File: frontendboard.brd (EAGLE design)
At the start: 160 x 100 mm, 65 parts, among them U1 MAX2769, X3 BU-SMA-H

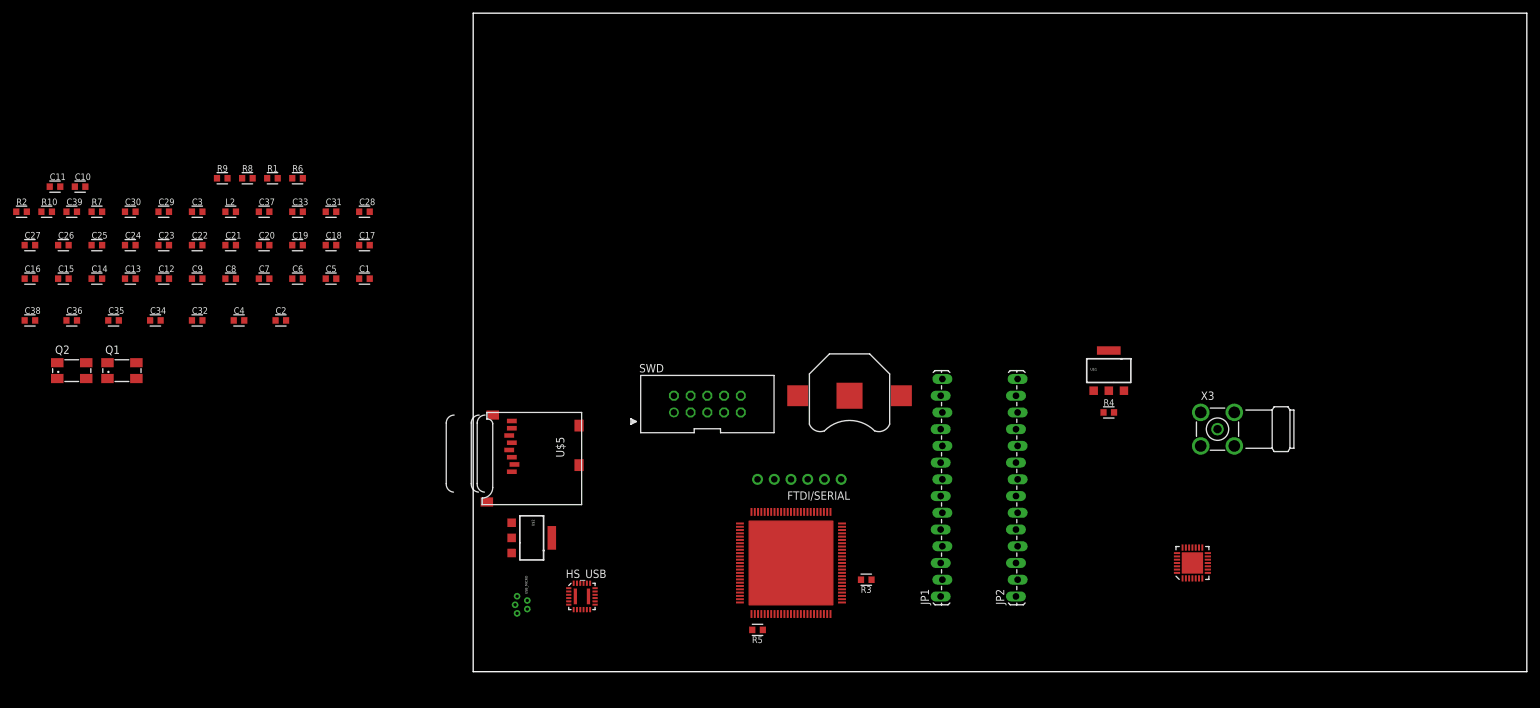
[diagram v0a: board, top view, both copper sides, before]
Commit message: Got all parts on the board for the layout. General sense of things.
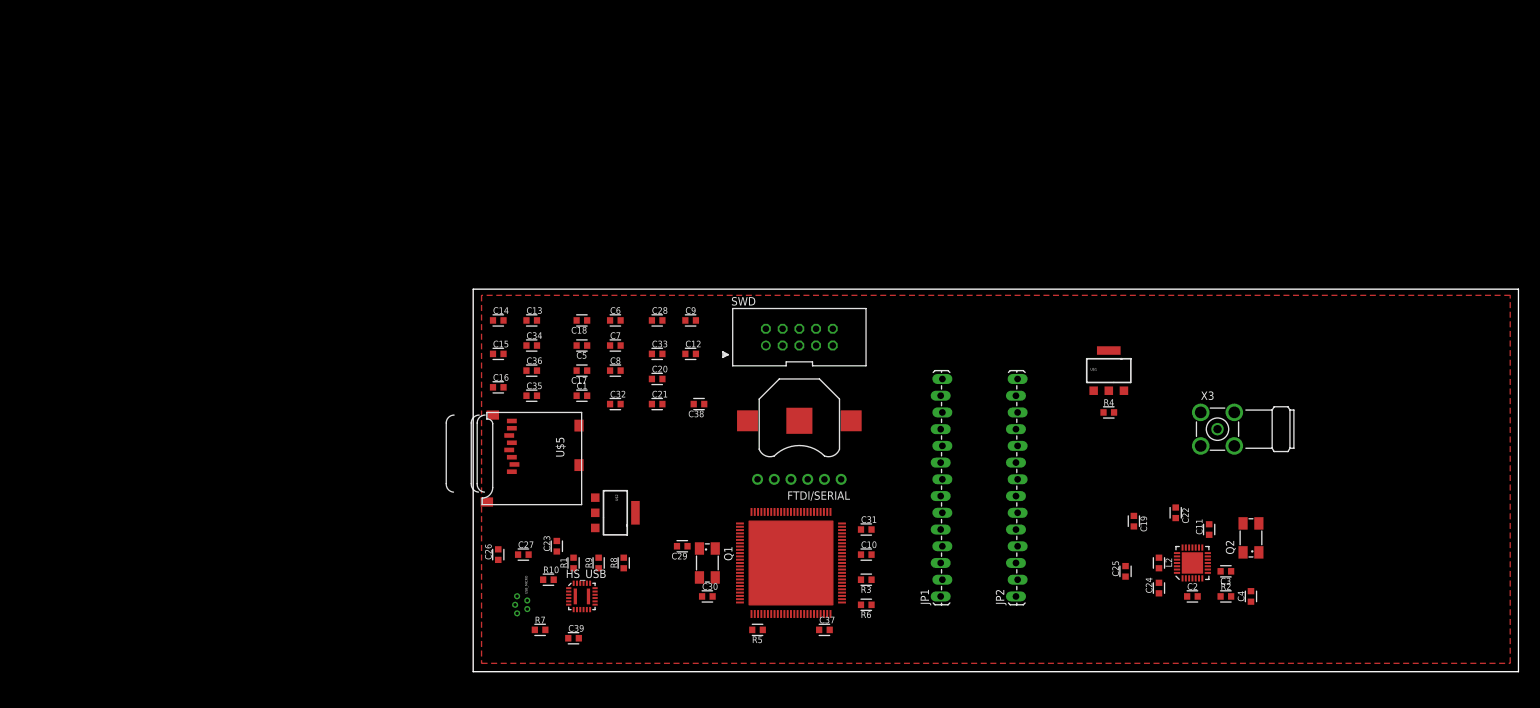
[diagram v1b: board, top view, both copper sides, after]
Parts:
- moved R2 192.0 mm to (114.3, 11.4)
- moved C11 182.8 mm to (111.8, 21.6), turned to 90 degrees
- moved Q2 180.9 mm to (118.1, 20.3), turned to 90 degrees
- moved C3 165.5 mm to (114.3, 15.2), turned to 180 degrees
- moved C24 164.7 mm to (104.1, 12.7), turned to 90 degrees
- moved C25 163.9 mm to (99.1, 15.2), turned to 90 degrees
- moved C4 159.3 mm to (118.1, 11.4), turned to 90 degrees
- moved C22 154.0 mm to (106.7, 24.1), turned to 270 degrees
- moved L2 150.7 mm to (104.1, 16.5), turned to 270 degrees
- moved C2 144.6 mm to (109.2, 11.4)
- moved C19 133.7 mm to (100.3, 22.9), turned to 270 degrees
- moved C10 131.8 mm to (59.7, 17.8)
- moved R6 108.0 mm to (59.7, 10.2), turned to 180 degrees
- moved C37 106.2 mm to (53.3, 6.35)
- moved C30 105.3 mm to (35.6, 11.4)
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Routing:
- added copper zone on layer 1, net BAR_GND
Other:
- board size 160 x 100 mm -> 158.7 x 58.1 mm

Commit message: Saving it before Andrew touches it.
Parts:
- removed C20: 0.1uF, rcl_custom:0603-B
- removed C21: 0.1nF, rcl_custom:0603-B
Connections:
- net 3.3VD: no longer C20.1, C21.1, Q2.1
- net BAR_GND: now also Q2.1; no longer C20.2, C21.2
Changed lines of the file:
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@@
 <element name="U$1" library="microbuilder" package="SOT223-R" value="" x="96.52" y="45.72"/>
 <element name="U$2" library="microbuilder" package="SOT223-R" value="" x="21.59" y="24.13" rot="R270"/>
-<element name="C20" library="rcl_custom" package="0603-B" value="0.1uF" x="27.94" y="44.45"/>
-<element name="C21" library="rcl_custom" package="0603-B" value="0.1nF" x="27.94" y="40.64"/>
 <element name="R4" library="rcl_custom" package="0603-B" value="20k" x="96.52" y="39.37"/>
 <element name="R5" library="rcl_custom" package="0603-B" value="20k" x="43.18" y="6.35" rot="R180"/>
@@
 <contactref element="U$2" pad="1"/>
 <contactref element="U$1" pad="1"/>
-<contactref element="C21" pad="2"/>
-<contactref element="C20" pad="2"/>
 <contactref element="R3" pad="1"/>
 <contactref element="R6" pad="1"/>
@@
 <vertex x="157.48" y="1.27"/>
 </polygon>
-<wire x1="58.89" y1="21.59" x2="56.01" y2="22.01" width="0" layer="19" extent="1-1"/>
+<contactref element="Q2" pad="1"/>
+<wire x1="118.11" y1="12.23" x2="119.31" y2="18.12" width="0" layer="19" extent="1-1"/>
+<wire x1="56.01" y1="22.01" x2="58.89" y2="21.59" width="0" layer="19" extent="1-1"/>
 <wire x1="17.51" y1="11.43" x2="19.05" y2="15.71" width="0" layer="19" extent="1-1"/>
 <wire x1="40.51" y1="13.01" x2="34.76" y2="11.43" width="0" layer="19" extent="1-1"/>
@@
 <contactref element="C9" pad="1"/>
 <contactref element="U1" pad="19"/>
-<contactref element="C20" pad="1"/>
-<contactref element="C21" pad="1"/>
-<contactref element="Q2" pad="1"/>
 <contactref element="R5" pad="2"/>
 <contactref element="HS_USB" pad="4"/>
@@
 <contactref element="C39" pad="2"/>
 <contactref element="U$3" pad="P$21"/>
-<wire x1="108.72" y1="18.85" x2="119.31" y2="18.12" width="0" layer="19" extent="1-1"/>
 <wire x1="56.01" y1="22.51" x2="108.72" y2="18.85" width="0" layer="19" extent="1-1"/>
 <wire x1="50.8" y1="29.21" x2="56.01" y2="22.51" width="0" layer="19" extent="1-1"/>
@@
 <wire x1="54.26" y1="8.76" x2="42.26" y2="8.76" width="0" layer="19" extent="1-1"/>
 <wire x1="33.49" y1="40.64" x2="42.26" y2="24.26" width="0" layer="19" extent="1-1"/>
-<wire x1="27.14" y1="40.64" x2="33.49" y2="40.64" width="0" layer="19" extent="1-1"/>
-<wire x1="27.14" y1="44.45" x2="27.14" y2="40.64" width="0" layer="19" extent="1-1"/>
-<wire x1="28.74" y1="48.26" x2="27.14" y2="44.45" width="0" layer="19" extent="1-1"/>
-<wire x1="22.39" y1="40.64" x2="27.14" y2="40.64" width="0" layer="19" extent="1-1"/>
+<wire x1="28.74" y1="48.26" x2="33.49" y2="40.64" width="0" layer="19" extent="1-1"/>
 <wire x1="28.74" y1="53.34" x2="28.74" y2="48.26" width="0" layer="19" extent="1-1"/>
 <wire x1="32.22" y1="53.34" x2="28.74" y2="53.34" width="0" layer="19" extent="1-1"/>
+<wire x1="22.39" y1="40.64" x2="28.74" y2="48.26" width="0" layer="19" extent="1-1"/>
 <wire x1="17.31" y1="41.91" x2="22.39" y2="40.64" width="0" layer="19" extent="1-1"/>
 <wire x1="17.31" y1="45.72" x2="17.31" y2="41.91" width="0" layer="19" extent="1-1"/>

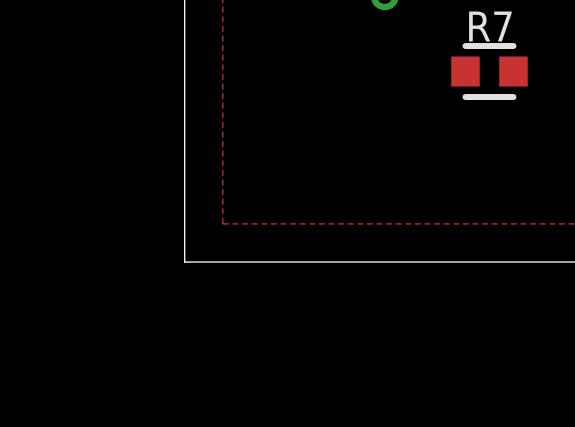
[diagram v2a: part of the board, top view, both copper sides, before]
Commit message: Add buses. Complete SDIO detect circuit. Add bypass caps where needed.
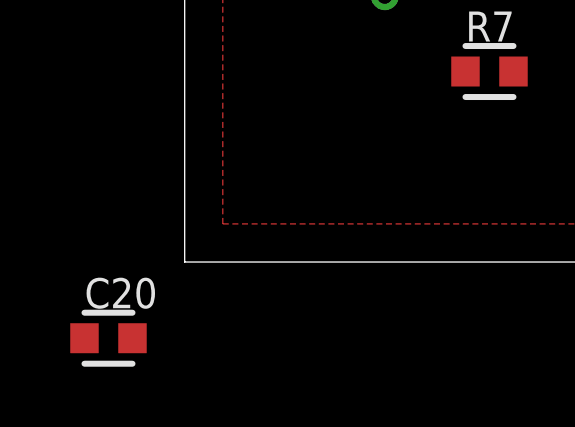
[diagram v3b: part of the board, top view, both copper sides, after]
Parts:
- added C20: 2.2uF, rcl_custom:0603-B
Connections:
- net 3.3VD: now also C20.2
- net BAR_GND: now also C20.1, U$5.CD2
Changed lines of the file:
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@@
 <attribute name="OC_FARNELL" value="unknown" x="163.83" y="81.28" size="1.778" layer="27" rot="R90" display="off"/>
 </element>
+<element name="C20" library="rcl_custom" package="0603-B" value="2.2uF" x="-2.54" y="-2.54"/>
 </elements>
 <signals>
@@
 </polygon>
 <contactref element="Q2" pad="1"/>
+<contactref element="C20" pad="1"/>
+<contactref element="U$5" pad="CD2"/>
+<wire x1="115.5799" y1="34.2801" x2="115.5799" y2="39.3799" width="0" layer="19" extent="1-1"/>
+<wire x1="110.4801" y1="39.3799" x2="115.5799" y2="39.3799" width="0" layer="19" extent="1-1"/>
+<wire x1="110.4801" y1="34.2801" x2="115.5799" y2="34.2801" width="0" layer="19" extent="1-1"/>
+<wire x1="119.31" y1="18.12" x2="115.5799" y2="34.2801" width="0" layer="19" extent="1-1"/>
 <wire x1="118.11" y1="12.23" x2="119.31" y2="18.12" width="0" layer="19" extent="1-1"/>
+<wire x1="113.5" y1="15.24" x2="118.11" y2="12.23" width="0" layer="19" extent="1-1"/>
+<wire x1="104.14" y1="13.5" x2="113.5" y2="15.24" width="0" layer="19" extent="1-1"/>
+<wire x1="99.06" y1="16.04" x2="104.14" y2="13.5" width="0" layer="19" extent="1-1"/>
+<wire x1="94.22" y1="42.67" x2="110.4801" y2="39.3799" width="0" layer="19" extent="1-1"/>
+<wire x1="60.49" y1="17.78" x2="99.06" y2="16.04" width="0" layer="19" extent="1-1"/>
+<wire x1="60.49" y1="13.97" x2="60.49" y2="17.78" width="0" layer="19" extent="1-1"/>
+<wire x1="60.49" y1="10.16" x2="60.49" y2="13.97" width="0" layer="19" extent="1-1"/>
+<wire x1="58.89" y1="21.59" x2="60.49" y2="17.78" width="0" layer="19" extent="1-1"/>
 <wire x1="56.01" y1="22.01" x2="58.89" y2="21.59" width="0" layer="19" extent="1-1"/>
+<wire x1="55.88" y1="29.21" x2="56.01" y2="22.01" width="0" layer="19" extent="1-1"/>
+<wire x1="52.54" y1="6.35" x2="60.49" y2="10.16" width="0" layer="19" extent="1-1"/>
+<wire x1="42.76" y1="8.76" x2="52.54" y2="6.35" width="0" layer="19" extent="1-1"/>
+<wire x1="40.51" y1="13.01" x2="42.76" y2="8.76" width="0" layer="19" extent="1-1"/>
+<wire x1="40.51" y1="18.01" x2="40.51" y2="13.01" width="0" layer="19" extent="1-1"/>
+<wire x1="34.76" y1="11.43" x2="40.51" y2="13.01" width="0" layer="19" extent="1-1"/>
+<wire x1="32.55" y1="19.05" x2="34.76" y2="11.43" width="0" layer="19" extent="1-1"/>
+<wire x1="22.86" y1="15.71" x2="32.55" y2="19.05" width="0" layer="19" extent="1-1"/>
+<wire x1="19.05" y1="15.71" x2="22.86" y2="15.71" width="0" layer="19" extent="1-1"/>
 <wire x1="17.51" y1="11.43" x2="19.05" y2="15.71" width="0" layer="19" extent="1-1"/>
-<wire x1="40.51" y1="13.01" x2="34.76" y2="11.43" width="0" layer="19" extent="1-1"/>
-<wire x1="42.76" y1="8.76" x2="40.51" y2="13.01" width="0" layer="19" extent="1-1"/>
-<wire x1="40.51" y1="18.01" x2="40.51" y2="13.01" width="0" layer="19" extent="1-1"/>
+<wire x1="15.51" y1="11.43" x2="17.51" y2="11.43" width="0" layer="19" extent="1-1"/>
+<wire x1="14.44" y1="5.08" x2="15.51" y2="11.43" width="0" layer="19" extent="1-1"/>
+<wire x1="12.7" y1="18.25" x2="19.05" y2="15.71" width="0" layer="19" extent="1-1"/>
+<wire x1="6.82" y1="17.78" x2="12.7" y2="18.25" width="0" layer="19" extent="1-1"/>
+<wire x1="3.81" y1="16.98" x2="6.82" y2="17.78" width="0" layer="19" extent="1-1"/>
+<wire x1="6.67" y1="8.86" x2="3.81" y2="16.98" width="0" layer="19" extent="1-1"/>
+<wire x1="2.07" y1="25.77" x2="3.81" y2="16.98" width="0" layer="19" extent="1-1"/>
+<wire x1="18.54" y1="26.43" x2="12.7" y2="18.25" width="0" layer="19" extent="1-1"/>
+<wire x1="16.07" y1="31.37" x2="18.54" y2="26.43" width="0" layer="19" extent="1-1"/>
+<wire x1="20.79" y1="40.64" x2="16.07" y2="31.37" width="0" layer="19" extent="1-1"/>
+<wire x1="15.71" y1="41.91" x2="20.79" y2="40.64" width="0" layer="19" extent="1-1"/>
+<wire x1="15.71" y1="45.72" x2="15.71" y2="41.91" width="0" layer="19" extent="1-1"/>
+<wire x1="15.71" y1="49.53" x2="15.71" y2="45.72" width="0" layer="19" extent="1-1"/>
+<wire x1="15.71" y1="53.34" x2="15.71" y2="49.53" width="0" layer="19" extent="1-1"/>
+<wire x1="22.39" y1="45.72" x2="20.79" y2="40.64" width="0" layer="19" extent="1-1"/>
+<wire x1="22.39" y1="49.53" x2="22.39" y2="45.72" width="0" layer="19" extent="1-1"/>
+<wire x1="22.39" y1="53.34" x2="22.39" y2="49.53" width="0" layer="19" extent="1-1"/>
+<wire x1="27.14" y1="53.34" x2="22.39" y2="53.34" width="0" layer="19" extent="1-1"/>
+<wire x1="27.14" y1="48.26" x2="22.39" y2="49.53" width="0" layer="19" extent="1-1"/>
+<wire x1="9.69" y1="53.34" x2="15.71" y2="53.34" width="0" layer="19" extent="1-1"/>
+<wire x1="8.09" y1="49.53" x2="9.69" y2="53.34" width="0" layer="19" extent="1-1"/>
+<wire x1="4.61" y1="48.26" x2="8.09" y2="49.53" width="0" layer="19" extent="1-1"/>
+<wire x1="8.09" y1="45.72" x2="8.09" y2="49.53" width="0" layer="19" extent="1-1"/>
+<wire x1="8.09" y1="41.91" x2="8.09" y2="45.72" width="0" layer="19" extent="1-1"/>
+<wire x1="4.61" y1="43.18" x2="8.09" y2="41.91" width="0" layer="19" extent="1-1"/>
+<wire x1="2.97" y1="38.97" x2="4.61" y2="43.18" width="0" layer="19" extent="1-1"/>
+<wire x1="5.47" y1="35.87" x2="2.97" y2="38.97" width="0" layer="19" extent="1-1"/>
+<wire x1="4.61" y1="53.34" x2="9.69" y2="53.34" width="0" layer="19" extent="1-1"/>
+<wire x1="33.82" y1="53.34" x2="27.14" y2="53.34" width="0" layer="19" extent="1-1"/>
+<wire x1="33.82" y1="48.26" x2="33.82" y2="53.34" width="0" layer="19" extent="1-1"/>
+<wire x1="35.09" y1="40.64" x2="33.82" y2="48.26" width="0" layer="19" extent="1-1"/>
+<wire x1="49.53" y1="38.1" x2="55.88" y2="29.21" width="0" layer="19" extent="1-1"/>
+<wire x1="49.53" y1="49.53" x2="49.53" y2="38.1" width="0" layer="19" extent="1-1"/>
+<wire x1="46.99" y1="49.53" x2="49.53" y2="49.53" width="0" layer="19" extent="1-1"/>
+<wire x1="54.61" y1="49.53" x2="49.53" y2="49.53" width="0" layer="19" extent="1-1"/>
+<wire x1="-3.34" y1="-2.54" x2="6.67" y2="8.86" width="0" layer="19" extent="1-1"/>
 </signal>
 <signal name="N$2">
@@
 <contactref element="C39" pad="2"/>
 <contactref element="U$3" pad="P$21"/>
+<contactref element="C20" pad="2"/>
 <wire x1="56.01" y1="22.51" x2="108.72" y2="18.85" width="0" layer="19" extent="1-1"/>
 <wire x1="50.8" y1="29.21" x2="56.01" y2="22.51" width="0" layer="19" extent="1-1"/>
@@
 <wire x1="10.96" y1="6.35" x2="14.51" y2="11.18" width="0" layer="19" extent="1-1"/>
 <wire x1="16.04" y1="5.08" x2="10.96" y2="6.35" width="0" layer="19" extent="1-1"/>
+<wire x1="-1.74" y1="-2.54" x2="10.96" y2="6.35" width="0" layer="19" extent="1-1"/>
 </signal>
 <signal name="N$3">

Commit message: All power pins replaced with customs so no ERC fails. Still needs BOOT0/PDR_ON on STM figured out.
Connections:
- removed net BODY: U1.BODY
- net BAR_GND: now also U1.BODY
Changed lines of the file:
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@@
 </elements>
 <signals>
-<signal name="BODY">
-<contactref element="U1" pad="BODY"/>
-</signal>
 <signal name="BAR_GND">
 <contactref element="X3" pad="4"/>
@@
 <contactref element="C20" pad="1"/>
 <contactref element="U$5" pad="CD2"/>
+<contactref element="U1" pad="BODY"/>
 <wire x1="115.5799" y1="34.2801" x2="115.5799" y2="39.3799" width="0" layer="19" extent="1-1"/>
 <wire x1="110.4801" y1="39.3799" x2="115.5799" y2="39.3799" width="0" layer="19" extent="1-1"/>
@@
 <wire x1="118.11" y1="12.23" x2="119.31" y2="18.12" width="0" layer="19" extent="1-1"/>
 <wire x1="113.5" y1="15.24" x2="118.11" y2="12.23" width="0" layer="19" extent="1-1"/>
-<wire x1="104.14" y1="13.5" x2="113.5" y2="15.24" width="0" layer="19" extent="1-1"/>
+<wire x1="109.22" y1="16.51" x2="113.5" y2="15.24" width="0" layer="19" extent="1-1"/>
+<wire x1="104.14" y1="13.5" x2="109.22" y2="16.51" width="0" layer="19" extent="1-1"/>
 <wire x1="99.06" y1="16.04" x2="104.14" y2="13.5" width="0" layer="19" extent="1-1"/>
 <wire x1="94.22" y1="42.67" x2="110.4801" y2="39.3799" width="0" layer="19" extent="1-1"/>
